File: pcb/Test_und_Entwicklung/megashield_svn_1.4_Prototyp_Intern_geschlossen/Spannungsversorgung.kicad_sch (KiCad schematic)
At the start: 21 parts, among them P24 +3.3VP, P29 9V S., P32 GND, P33 5V, P34 3,3V, P38 +5VP, P45 GND, P47 9V, U1 DC 9V, U6 LM2940CS-5.0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

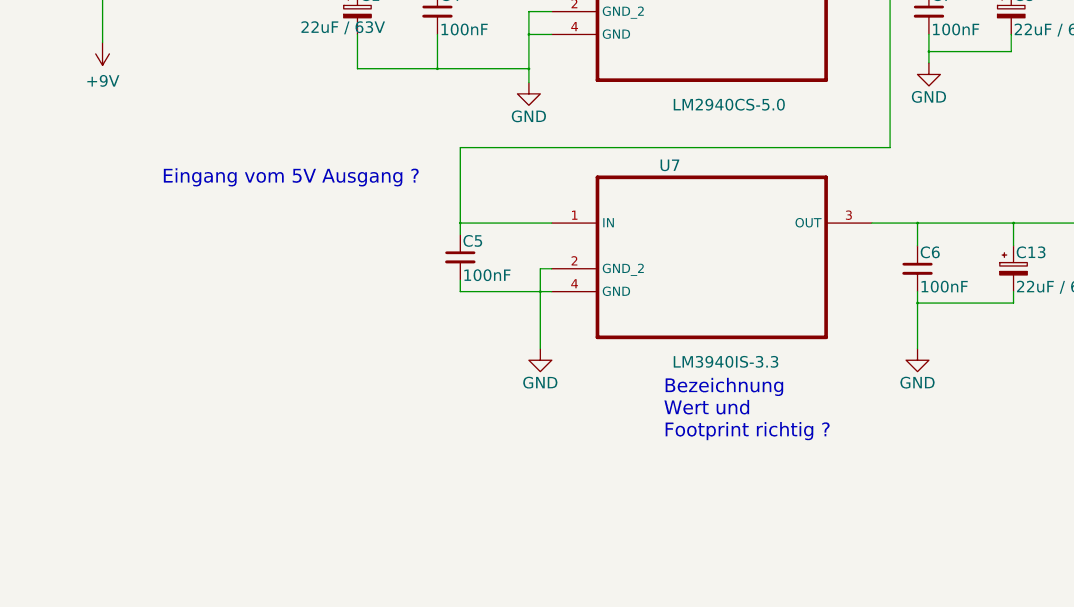
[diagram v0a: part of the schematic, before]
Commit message: megashield_svn_1.4_Prototyp_Intern_geschlossen
megashield_svn_1.4_Prototyp_Intern_geschlossen
3D Kicad Symbolpfade angepasst
Anmerkungen in Schaltplan zu den Änderungen der 1.4 Platine entfernt
Schaltplan als PDF erstellt
Datei Leichen in Archiv verschoben
Unterordner für Datenblättererstellt
Unterordner für Produktionsdaten erstellt
Schaltplan und Platinen Layout Kicad Format geändert (von Kicad automatisch geändert)
+ Am Schaltplan und dem Platinen Layout wurden keine Änderungen vorgenommen+
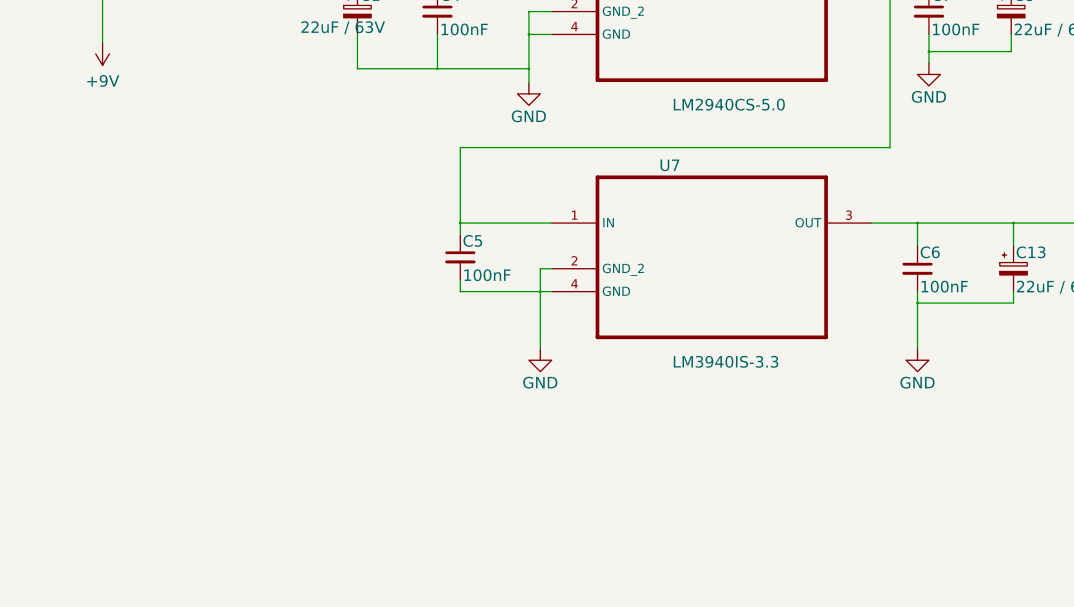
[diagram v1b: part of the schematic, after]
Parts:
- C1, C13, C8: Bestücken (Assemble) NEIN (NO) -> (none)
- C4, C5, C6, C7: Gehäuseart 0805 -> (none)
- D4: Bestücken (Assemble) JA (YES) -> (none); Reichelt-Bestellnummer R: S 1G SMD -> (none)
- F1: Bestücken (Assemble) JA (YES) -> (none); JLCPCB Basic / Extern 1 -> (none); Reichelt-Bestellnummer R: OMH 125 HALTER -> (none)
- U6: JLCPCB Basic / Extern 1 -> (none)
- U7: Bestücken (Assemble) JA (YES) -> (none); Funktion LDO voltage regulator, fixed, 3.3 Vout, 1 A, D2PAK -> (none); JLCPCB Basic / Extern 1 -> (none); Reichelt-Bestellnummer R: LM 3940 IS3,3 -> (none)
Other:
- note removed: "Bezeichnung Wert und Footprint richtig ?"
- note removed: "Eingang vom 5V Ausgang ?"
